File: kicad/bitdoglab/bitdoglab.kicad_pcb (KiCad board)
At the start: 2 copper layers, 87.9 x 123.9 mm, 60 parts, among them J1 Conn_01x20_Socket, J10 3V3, J11 5V-VSYS, J12 Conn_01x05_Pin, J13 Conn_01x05_Pin, J14 5x5 Matrix led, J15 0, J16 1, J17 2, J18 3, J19 JOYSTICK, J2 conector_idc, J20 Conn_01x04_Pin, J21 Conn_01x04_Pin, J22 Conn_01x04_Pin, J3 Conn_01x20_Socket, J4 jumper_mic, J5 Conn_01x05_Pin, J6 Conn_01x05_Pin, J7 GND, J8 ANA-IN, J9 GND, Q1 DMG2305UX-13, Q2 BC337, Q3 BC337, SW1 Reset, SW2 Botão, SW3 Button_B, U1 3.3v_tht, U4 MIC

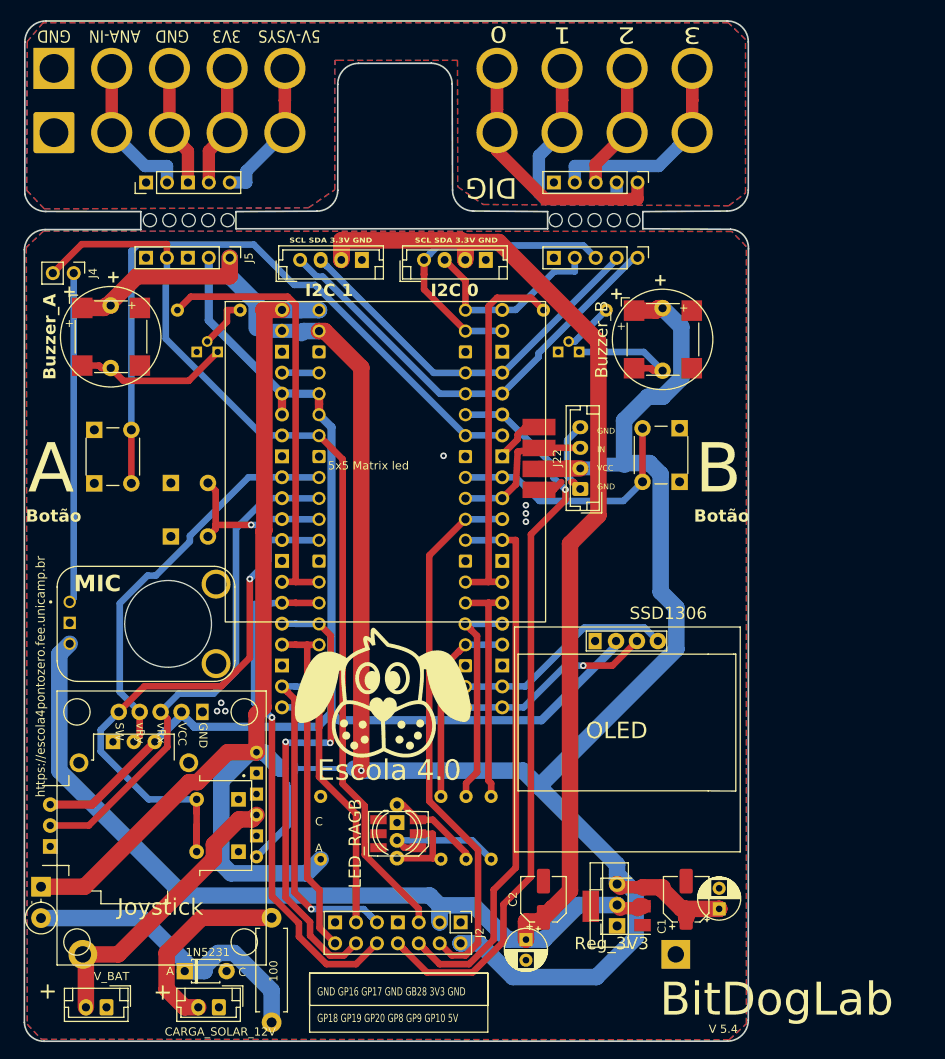
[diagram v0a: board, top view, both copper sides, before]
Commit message: change buttons footprints for 12mm
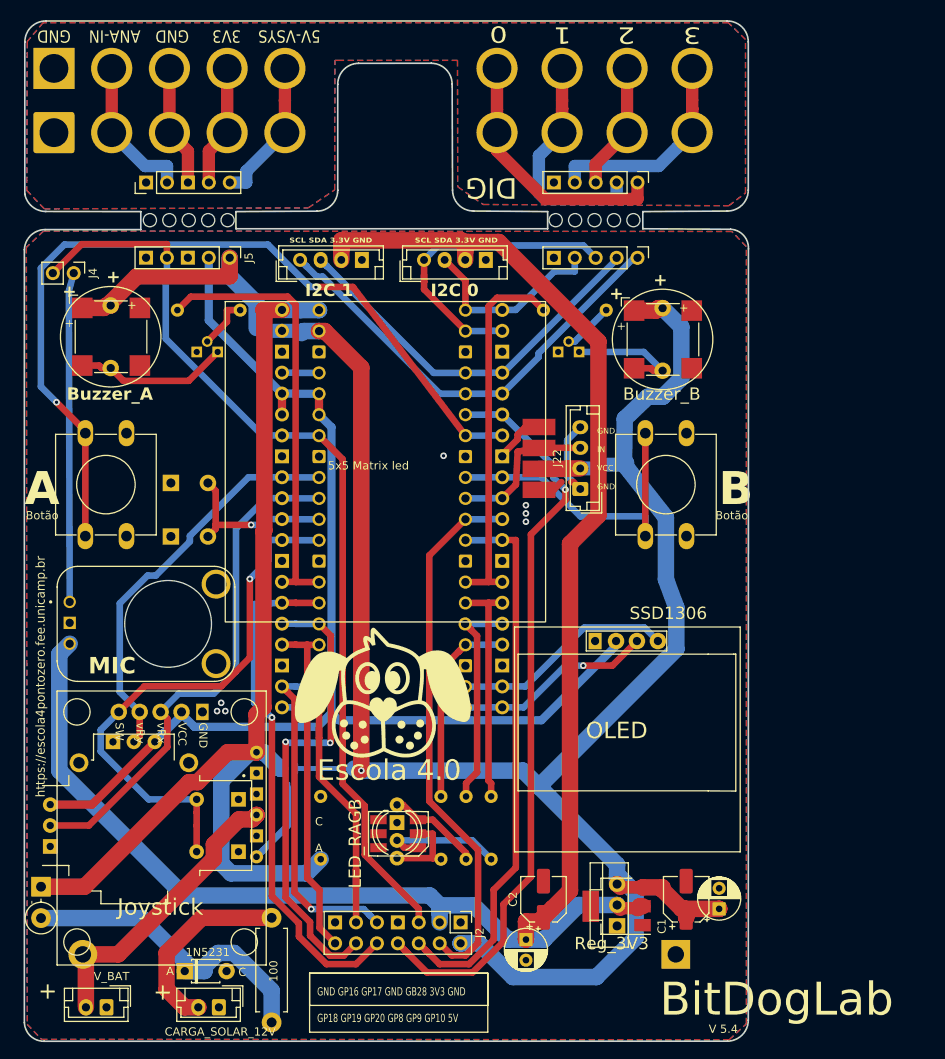
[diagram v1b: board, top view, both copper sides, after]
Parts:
- SW2: footprint Button_Switch_THT:SW_PUSH_6mm -> Button_Switch_THT:SW_PUSH-12mm
- SW3: value Button_B -> Botão; footprint Button_Switch_THT:SW_PUSH_6mm -> Button_Switch_THT:SW_PUSH-12mm
- moved SW2 14.1 mm to (95.5, 94.8), turned to 90 degrees
- moved SW3 6.60 mm to (163.5, 94.8)
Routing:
- net /pino_07: track 83.2 -> 103.3 mm, vias 0 -> 2
- net /pino_09: track 30.2 -> 38.7 mm
- net /GP0_EXT: track 34.1 -> 26.7 mm
- net VSYS_EXT: track 23.7 -> 17.8 mm
- net /GP03_EXT: track 36.8 -> 31.8 mm
- net /GP02_EXT: track 33.9 -> 29.0 mm
- net /pino_29: track 70.9 -> 66.1 mm
- net /GP16: track 39.2 -> 35.8 mm
- net VSYS: track 279.8 -> 276.8 mm
- net /GP01: track 40.3 -> 38.3 mm
- net /GP17: track 43.6 -> 41.9 mm
- net +3.3V: track 222.2 -> 220.6 mm
- net /AGND_EXT: track 14.8 -> 16.4 mm
- net 3.3_OUT_EXT: track 14.8 -> 16.4 mm
- net /GP03: track 54.8 -> 55.9 mm
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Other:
- board text removed: "Botão"
